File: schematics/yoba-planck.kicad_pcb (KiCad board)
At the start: 2 copper layers, 111.2 x 73.2 mm, 112 parts, among them M1 AUDIO-JACK3, M2 AUDIO-JACK3, M3 ARDUINO_PRO_MICRO, Q1 BS170, SW1 SW_PUSH, SW10 SW_PUSH, SW11 SW_PUSH, SW12 SW_PUSH, SW13 SW_PUSH, SW14 SW_PUSH, SW15 SW_PUSH, SW16 SW_PUSH, SW17 SW_PUSH, SW18 SW_PUSH, SW19 SW_PUSH, SW2 SW_PUSH, SW20 SW_PUSH, SW21 SW_PUSH, SW22 SW_PUSH, SW23 SW_PUSH, SW24 SW_PUSH, SW3 SW_PUSH, SW4 SW_PUSH, SW5 SW_PUSH, SW6 SW_PUSH, SW7 SW_PUSH, SW8 SW_PUSH, SW9 SW_PUSH

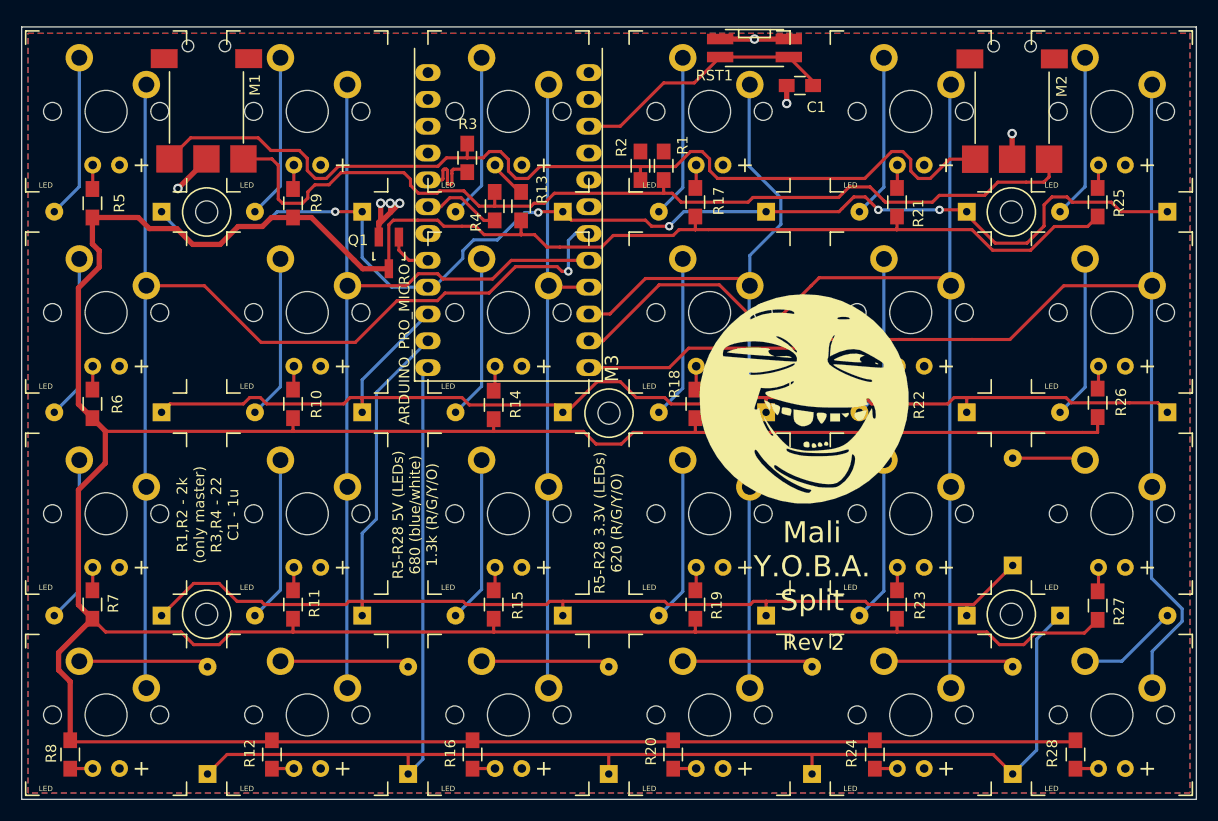
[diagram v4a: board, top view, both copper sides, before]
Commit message: yoba rev3 to smd
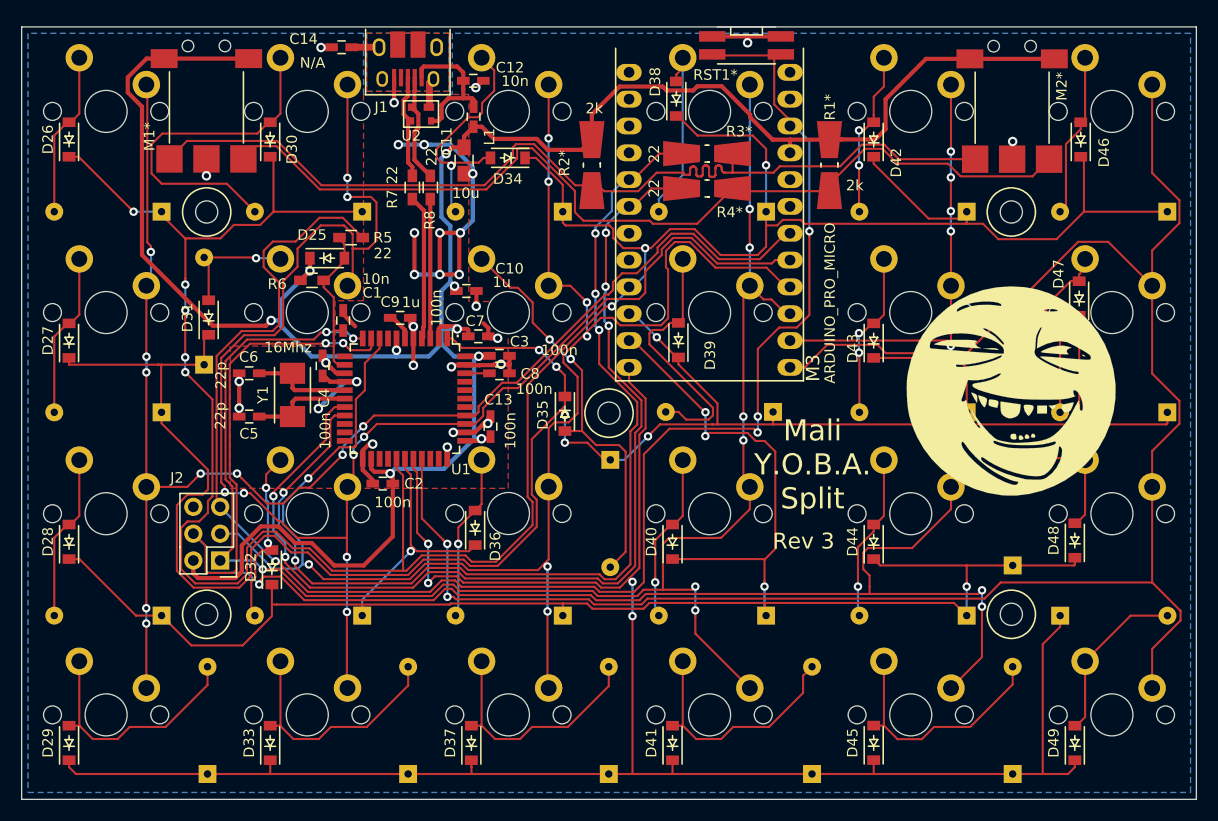
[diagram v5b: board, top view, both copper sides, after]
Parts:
- removed Q1: BS170, TO_SOT_Packages_SMD:SOT-23_Handsoldering
- removed R1, R2: 2k, Resistors_SMD:R_0805_HandSoldering
- removed R10, R11, R12, R13, R14, R15, R16, R17, R18, R19, R20, R21, R22, R23, R24, R25, R26, R27, R28, R9: 1k, Resistors_SMD:R_0805_HandSoldering
- removed R3, R4: 22, Resistors_SMD:R_0805_HandSoldering
- added C10: 1u, Capacitors_SMD:C_0603_HandSoldering, F.Cu at (148.1, 87.0)
- added C11: 10u, Capacitors_SMD:C_0805_HandSoldering, F.Cu at (147.9, 74.7)
- added C12: 10n, Capacitors_SMD:C_0603_HandSoldering, F.Cu at (148.8, 67.1)
- added C13: 100n, Capacitors_SMD:C_0603_HandSoldering, F.Cu at (150.4, 99.8)
- added C14: N/A, Capacitors_SMD:C_0603_HandSoldering, F.Cu at (136.3, 63.9)
- added C2: 100n, Capacitors_SMD:C_0603_HandSoldering, F.Cu at (140.2, 105.2)
- added C3: 100n, Capacitors_SMD:C_0603_HandSoldering, F.Cu at (151.2, 93.2)
- added C4: 100n, Capacitors_SMD:C_0603_HandSoldering, F.Cu at (134.5, 94.1)
- added C5: 22p, Capacitors_SMD:C_0603_HandSoldering, F.Cu at (127.5, 98.9)
- added C6: 22p, Capacitors_SMD:C_0603_HandSoldering, F.Cu at (127.5, 94.8)
- added C7: 100n, Capacitors_SMD:C_0603_HandSoldering, F.Cu at (149.2, 91.3)
- added C8: 100n, Capacitors_SMD:C_0603_HandSoldering, F.Cu at (151.2, 94.8)
- added C9: 1u, Capacitors_SMD:C_0603_HandSoldering, F.Cu at (141.8, 89.5)
- added D49: D, Diodes_SMD:SOD-123, F.Cu at (205.7, 129.8)
- added J1: USB_OTG, Connect:USB_Micro-B_10103594-0001LF, F.Cu at (142.6, 65.3)
- added J2: Conn_02x03_Odd_Even, Pin_Headers:Pin_Header_Straight_2x03, F.Cu at (124.8, 112.5)
- added L1: Ferrite_Bead_Small, Capacitors_SMD:C_0603_HandSoldering, F.Cu at (148.8, 70.5)
- added R1*: 2k, Resistors_Universal:Resistor_SMDuniversal_0805to1206_HandSoldering, F.Cu at (182.5, 75.1)
- added R2*: 2k, Resistors_Universal:Resistor_SMDuniversal_0805to1206_HandSoldering, F.Cu at (160.0, 75.1)
- added R3*: 22, Resistors_Universal:Resistor_SMDuniversal_0805to1206_HandSoldering, F.Cu at (170.9, 74.0)
- added R4*: 22, Resistors_Universal:Resistor_SMDuniversal_0805to1206_HandSoldering, F.Cu at (170.9, 77.3)
- added U1: ATmega32U4-AU, Housings_QFP:TQFP-44_10x10mm_Pitch0.8mm, F.Cu at (142.3, 97.2)
- added U2: PRTR5V0U2X, yoba:SOT143B, F.Cu at (143.8, 70.2)
- added Y1: 16Mhz, Crystals:Crystal_SMD_5032_2Pads, F.Cu at (131.7, 96.8)
- C1: value C -> 10n; footprint Capacitors_SMD:C_0805_HandSoldering -> Capacitors_SMD:C_0603_HandSoldering
- D25: value LED -> 1N4148; footprint mx1a:MX1A-led -> Diodes_SMD:SOD-123
- D26, D27, D28, D29, D30, D31, D32, D33, D34, D35, D36, D37, D38, D39, D40, D41, D42, D43, D44, D45, D46, D47, D48: value LED -> D; footprint mx1a:MX1A-led -> Diodes_SMD:SOD-123
- R5, R7, R8: value 1k -> 22; footprint Resistors_SMD:R_0805_HandSoldering -> Resistors_SMD:R_0603_HandSoldering
- R6: value 1k -> 2k; footprint Resistors_SMD:R_0805_HandSoldering -> Resistors_SMD:R_0603_HandSoldering
- moved D29 63.9 mm to (110.5, 129.8), turned to 90 degrees
- moved D33 63.9 mm to (129.5, 129.8), turned to 90 degrees
- moved D37 63.9 mm to (148.6, 129.8), turned to 90 degrees
- moved D41 63.9 mm to (167.6, 129.8), turned to 90 degrees
- moved D45 63.9 mm to (186.7, 129.8), turned to 90 degrees
- moved R8 63.6 mm to (144.7, 77.2), turned to 90 degrees
- moved R7 49.8 mm to (143.0, 77.2)
- moved C1 48.6 mm to (136.4, 89.8), turned to 270 degrees
- moved D25 25.1 mm to (134.9, 83.9)
- moved R5 24.7 mm to (137.2, 82.0), turned to 180 degrees
- moved R6 23.9 mm to (133.5, 86.0), turned to 0 degrees
- moved D31 20.8 mm to (123.7, 89.5), turned to 90 degrees
- moved D47 20.6 mm to (206.2, 87.7), turned to 90 degrees
- moved D38 20.5 mm to (168.0, 68.8), turned to 90 degrees
- moved G*** 19.6 mm to (199.8, 96.5)
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- renumbered M1 to M1*, M2 to M2*, RST1 to RST1*
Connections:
- net col2 renamed col2/sck
- net col3 renamed col3/miso
- net col4 renamed col4/mosi
- D25 pad 1: Net-(D25-Pad1) -> VCC
- D25 pad 2: VCC -> Net-(C1-Pad2)
- D26 pad 1: Net-(D26-Pad1) -> row0
- D26 pad 2: VCC -> Net-(D1-Pad2)
- D27 pad 1: Net-(D27-Pad1) -> row1
- D27 pad 2: VCC -> Net-(D2-Pad2)
- D28 pad 1: Net-(D28-Pad1) -> row2
- D28 pad 2: VCC -> Net-(D28-Pad2)
- D29 pad 1: Net-(D29-Pad1) -> row3
- D29 pad 2: VCC -> Net-(D29-Pad2)
- D3 pad 2: Net-(D3-Pad2) -> Net-(D28-Pad2)
- D30 pad 1: Net-(D30-Pad1) -> row0
- D30 pad 2: VCC -> Net-(D30-Pad2)
- D31 pad 1: Net-(D31-Pad1) -> row1
- D31 pad 2: VCC -> Net-(D31-Pad2)
- D32 pad 1: Net-(D32-Pad1) -> row2
- D32 pad 2: VCC -> Net-(D32-Pad2)
- D33 pad 1: Net-(D33-Pad1) -> row3
- D33 pad 2: VCC -> Net-(D33-Pad2)
- D34 pad 1: Net-(D34-Pad1) -> row0
- D34 pad 2: VCC -> Net-(D34-Pad2)
- D35 pad 1: Net-(D35-Pad1) -> row1
- D35 pad 2: VCC -> Net-(D10-Pad2)
- D36 pad 1: Net-(D36-Pad1) -> row2
- D36 pad 2: VCC -> Net-(D11-Pad2)
- D37 pad 1: Net-(D37-Pad1) -> row3
- D37 pad 2: VCC -> Net-(D12-Pad2)
- D38 pad 1: Net-(D38-Pad1) -> row0
- D38 pad 2: VCC -> Net-(D13-Pad2)
- D39 pad 1: Net-(D39-Pad1) -> row1
- D39 pad 2: VCC -> Net-(D14-Pad2)
- D4 pad 2: Net-(D4-Pad2) -> Net-(D29-Pad2)
- D40 pad 1: Net-(D40-Pad1) -> row2
- D40 pad 2: VCC -> Net-(D15-Pad2)
- D41 pad 1: Net-(D41-Pad1) -> row3
- D41 pad 2: VCC -> Net-(D16-Pad2)
- D42 pad 1: Net-(D42-Pad1) -> row0
- D42 pad 2: VCC -> Net-(D17-Pad2)
- D43 pad 1: Net-(D43-Pad1) -> row1
- D43 pad 2: VCC -> Net-(D18-Pad2)
- D44 pad 1: Net-(D44-Pad1) -> row2
- D44 pad 2: VCC -> Net-(D19-Pad2)
- D45 pad 1: Net-(D45-Pad1) -> row3
- D45 pad 2: VCC -> Net-(D20-Pad2)
- D46 pad 1: Net-(D46-Pad1) -> row0
- D46 pad 2: VCC -> Net-(D21-Pad2)
- D47 pad 1: Net-(D47-Pad1) -> row1
- D47 pad 2: VCC -> Net-(D22-Pad2)
- D48 pad 1: Net-(D48-Pad1) -> row2
- D48 pad 2: VCC -> Net-(D23-Pad2)
- D5 pad 2: Net-(D5-Pad2) -> Net-(D30-Pad2)
- D6 pad 2: Net-(D6-Pad2) -> Net-(D31-Pad2)
- D7 pad 2: Net-(D7-Pad2) -> Net-(D32-Pad2)
- D8 pad 2: Net-(D8-Pad2) -> Net-(D33-Pad2)
- D9 pad 2: Net-(D9-Pad2) -> Net-(D34-Pad2)
- M3 pad 1: (no net) -> Net-(M3-Pad1)
- M3 pad 19: (no net) -> Net-(M3-Pad19)
- M3 pad 2: (no net) -> Net-(M3-Pad2)
- M3 pad 20: (no net) -> Net-(M3-Pad20)
- M3 pad 22: Net-(C1-Pad2) -> rst
- M3 pad 24: (no net) -> Net-(M3-Pad24)
- M3 pad 7: (no net) -> Net-(M3-Pad7)
- M3 pad 8: backlight -> Net-(M3-Pad8)
- R5 pad 1: Net-(Q1-Pad1) -> rst
- R5 pad 2: Net-(D25-Pad1) -> Net-(C1-Pad2)
- R6 pad 1: Net-(Q1-Pad1) -> VCC
- R6 pad 2: Net-(D26-Pad1) -> Net-(C1-Pad2)
- R7 pad 1: Net-(Q1-Pad1) -> d+
- R7 pad 2: Net-(D27-Pad1) -> /ud+
- R8 pad 1: Net-(Q1-Pad1) -> d-
- R8 pad 2: Net-(D28-Pad1) -> /ud-
- RST1* pad 2: Net-(C1-Pad2) -> rst
- SW3 pad 2: Net-(D3-Pad2) -> Net-(D28-Pad2)
- SW4 pad 2: Net-(D4-Pad2) -> Net-(D29-Pad2)
- SW5 pad 2: Net-(D5-Pad2) -> Net-(D30-Pad2)
- SW6 pad 2: Net-(D6-Pad2) -> Net-(D31-Pad2)
- SW7 pad 2: Net-(D7-Pad2) -> Net-(D32-Pad2)
- SW8 pad 2: Net-(D8-Pad2) -> Net-(D33-Pad2)
- SW9 pad 2: Net-(D9-Pad2) -> Net-(D34-Pad2)
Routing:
- net Net-(Q1-Pad1): track 468.4 -> 0.00 mm
- net VCC: track 0.00 -> 239.6 mm, vias 0 -> 10
- net rst: track 0.00 -> 156.3 mm, vias 0 -> 4
- net row0: track 114.2 -> 265.2 mm, vias 5 -> 8
- net col4/mosi: track 98.1 -> 203.7 mm, vias 0 -> 13
- net row1: track 117.0 -> 216.5 mm, vias 0 -> 6
- net col2/sck: track 61.3 -> 155.0 mm, vias 0 -> 8
- net sda: track 7.37 -> 98.4 mm, vias 0 -> 5
- net scl: track 9.40 -> 97.0 mm, vias 0 -> 5
- net col3/miso: track 76.7 -> 155.3 mm, vias 0 -> 9
- net col5: track 116.2 -> 188.4 mm, vias 0 -> 2
- net row2: track 119.0 -> 190.7 mm, vias 0 -> 5
- net col1: track 81.6 -> 148.7 mm, vias 0 -> 8
- net GND: track 21.7 -> 88.6 mm, vias 7 -> 29
- net row3: track 139.5 -> 191.5 mm, vias 0 -> 4
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- added copper zone on B.Cu, net /shld
- added copper zone on F.Cu, net /shld
- added copper zone on F.Cu, net GND
- removed copper zone on F.Cu, net VCC
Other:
- net class Default: clearance 0.3 -> 0.195; trace_width 0.3 -> 0.2
- net class crystal added: clearance 0.2, trace_width 0.4, via_dia 0.8, via_drill 0.4
- net class power: clearance 0.3 -> 0.195; trace_width 0.5 -> 0.4
- net class shield added: clearance 0.22, trace_width 0.65, via_dia 0.8, via_drill 0.4
- net class usb added: clearance 0.195, trace_width 0.4, via_dia 0.8, via_drill 0.4
- rule trace_clearance: 0.3 -> 0.195
- rule trace_min: 0.3 -> 0.2
- board text added: "."
- board text added: "Rev 3"
- board text removed: "+"
- board text removed: "R1,R2 - 2k (only master) R3,R4 - 22 C1 - 1u"
- board text removed: "R5-R28 3.3V (LEDs) 620 (R/G/Y/O)"
- board text removed: "R5-R28 5V (LEDs) 680 (blue/white) 1.3k (R/G/Y/O)"
- board text removed: "Rev 2"

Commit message: fixed vbus sense line for atmega32u4
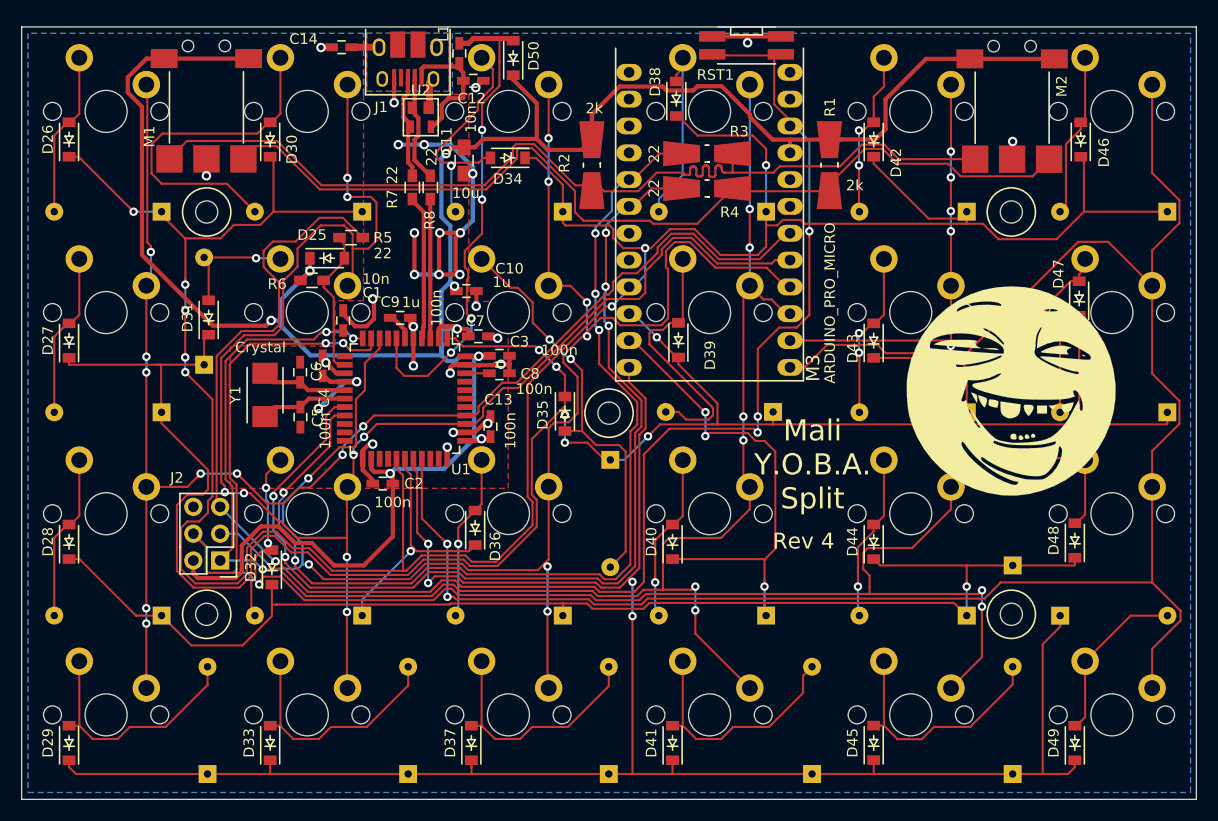
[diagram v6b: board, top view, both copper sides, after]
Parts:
- added D50: D, Diodes_SMD:SOD-123, F.Cu at (152.6, 64.9)
- C14: value N/A -> 100n
- Y1: value 16Mhz -> Crystal
- moved L1 6.15 mm to (147.4, 64.5), turned to 90 degrees
- moved C5 4.85 mm to (132.4, 99.0), turned to 270 degrees
- moved C6 4.83 mm to (132.4, 94.7), turned to 90 degrees
- moved Y1 2.60 mm to (129.1, 96.8)
- moved U2 0.30 mm to (143.8, 70.5)
- renumbered M1* to M1, M2* to M2, R1* to R1, R2* to R2, R3* to R3, R4* to R4, RST1* to RST1
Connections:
- L1 pad 2: VCC -> /vbussens
- U1 pad 7: VCC -> /vbussens
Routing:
- net /vbussens: track 0.00 -> 46.8 mm, vias 0 -> 4
- net VCC: track 239.6 -> 245.2 mm, vias 10 -> 9
- net /vbus: track 13.9 -> 12.4 mm
- net Net-(C6-Pad1): track 9.58 -> 8.21 mm
- net Net-(C5-Pad1): track 9.62 -> 8.25 mm
- net Net-(D34-Pad2): track 23.3 -> 22.4 mm
- net GND: track 88.6 -> 88.1 mm, vias 29 -> 28
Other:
- board text added: "Rev 4"
- board text removed: "Rev 3"
